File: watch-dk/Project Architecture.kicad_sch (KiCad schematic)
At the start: 0 parts

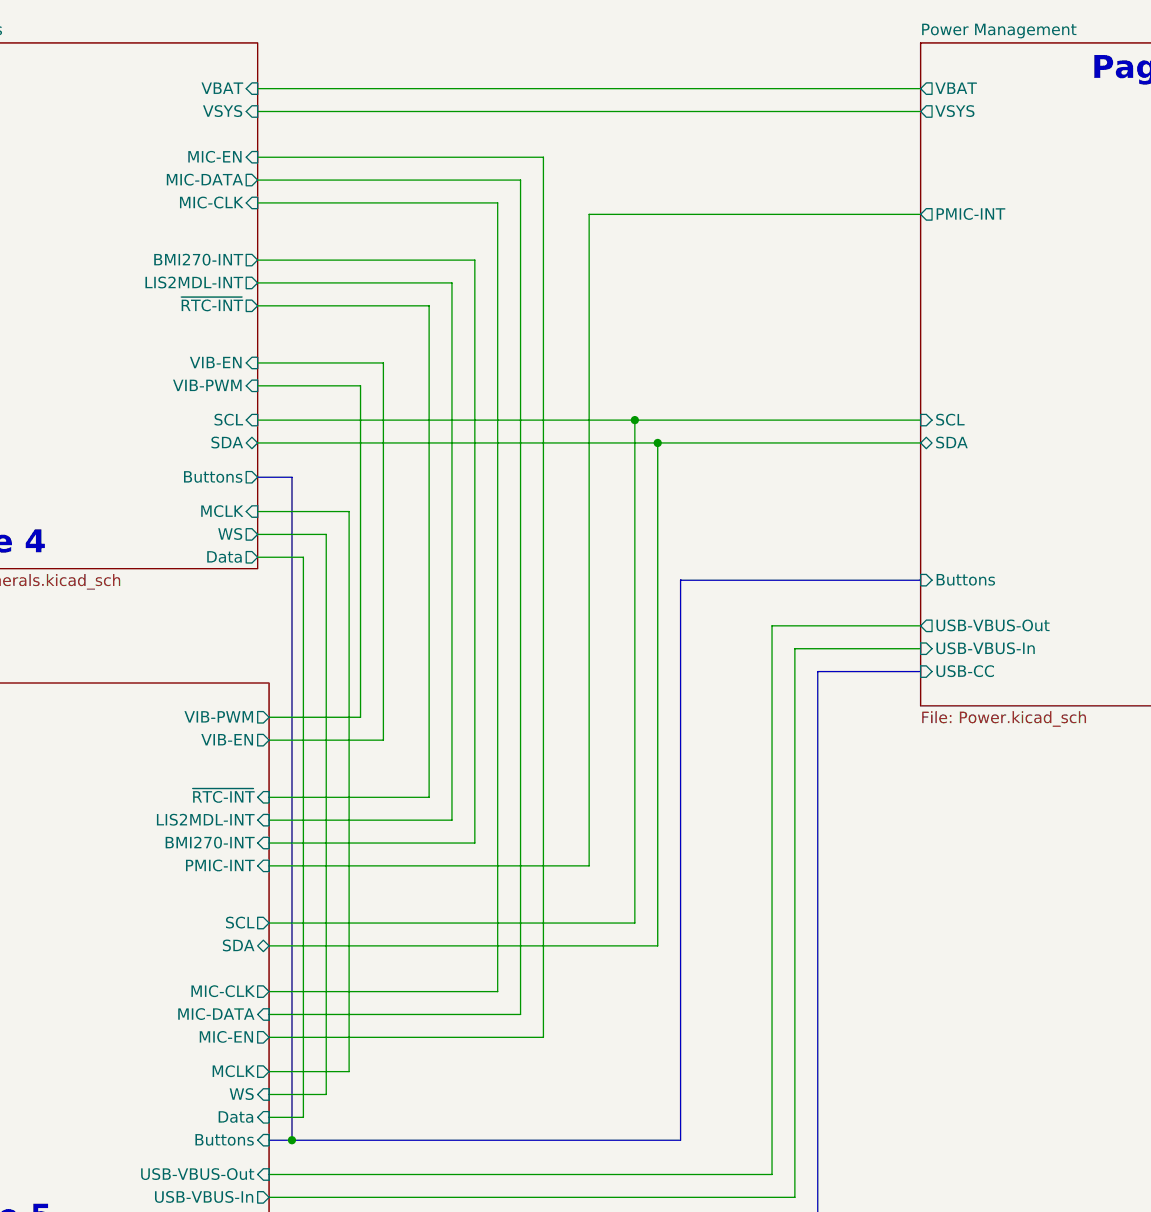
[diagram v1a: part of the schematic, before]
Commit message: Feature: Issue #145
- Update symbols

Signed-off-by: Daniel Kampert <DanielKampert@kampis-elektroecke.de>
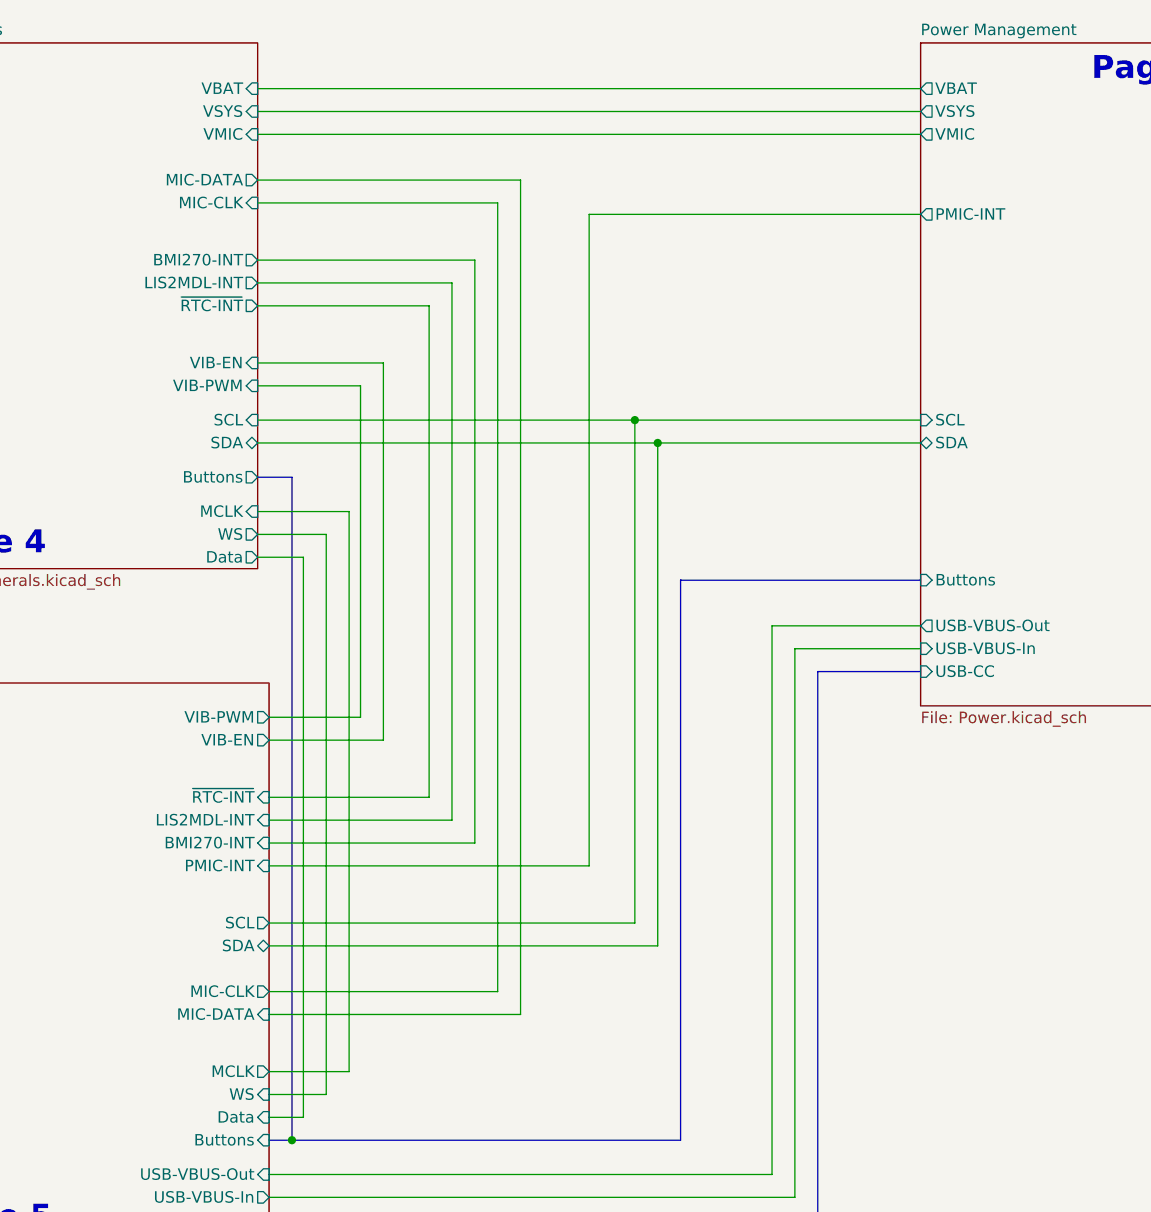
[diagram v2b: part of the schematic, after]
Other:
- sheet MCU ports: added none; removed MIC-EN
- sheet Peripherals ports: added VMIC; removed MIC-EN
- sheet Power Management ports: added VMIC; removed none
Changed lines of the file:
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@@
+	(wire
+		(pts
+			(xy 81.28 27.94) (xy 154.94 27.94)
+		)
+		(stroke
+			(width 0)
+			(type default)
+		)
+	)
 	(wire
 		(pts
@@
 		)
 	)
-	(wire
-		(pts
-			(xy 113.03 128.27) (xy 82.55 128.27)
-		)
-		(stroke
-			(width 0)
-			(type default)
-		)
-	)
 	(bus
 		(pts
@@
 		(pts
 			(xy 107.95 123.19) (xy 107.95 35.56)
-		)
-		(stroke
-			(width 0)
-			(type default)
-		)
-	)
-	(wire
-		(pts
-			(xy 81.28 30.48) (xy 113.03 30.48)
-		)
-		(stroke
-			(width 0)
-			(type default)
-		)
-	)
-	(wire
-		(pts
-			(xy 113.03 30.48) (xy 113.03 128.27)
 		)
 		(stroke
@@
 			)
 		)
-		(pin "MIC-EN" input
-			(at 81.28 30.48 0)
-			(effects
-				(font
-					(size 1.27 1.27)
-				)
-				(justify right)
-			)
-		)
 		(pin "MIC-CLK" input
 			(at 81.28 35.56 0)
@@
 		(pin "Data" output
 			(at 81.28 74.93 0)
+			(effects
+				(font
+					(size 1.27 1.27)
+				)
+				(justify right)
+			)
+		)
+		(pin "VMIC" input
+			(at 81.28 27.94 0)
 			(effects
 				(font
@@
 			)
 		)
-		(pin "MIC-EN" output
-			(at 82.55 128.27 0)
-			(effects
-				(font
-					(size 1.27 1.27)
-				)
-				(justify right)
-			)
-		)
 		(pin "USB-VBUS-In" output
 			(at 82.55 146.05 0)
@@
 			(effects
 				(font
+					(size 1.27 1.27)
+				)
+				(justify left)
+			)
+		)
+		(pin "VMIC" output
+			(at 154.94 27.94 180)
+			(effects
+				(font
